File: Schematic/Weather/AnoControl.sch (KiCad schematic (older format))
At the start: 6 parts, among them J10 5_Way_Wire, J11 5_Way_Wire, J12 5_Way_Wire, J13 5_Way_Wire, J8 3_Way_Wire, J9 4_Way_Wire

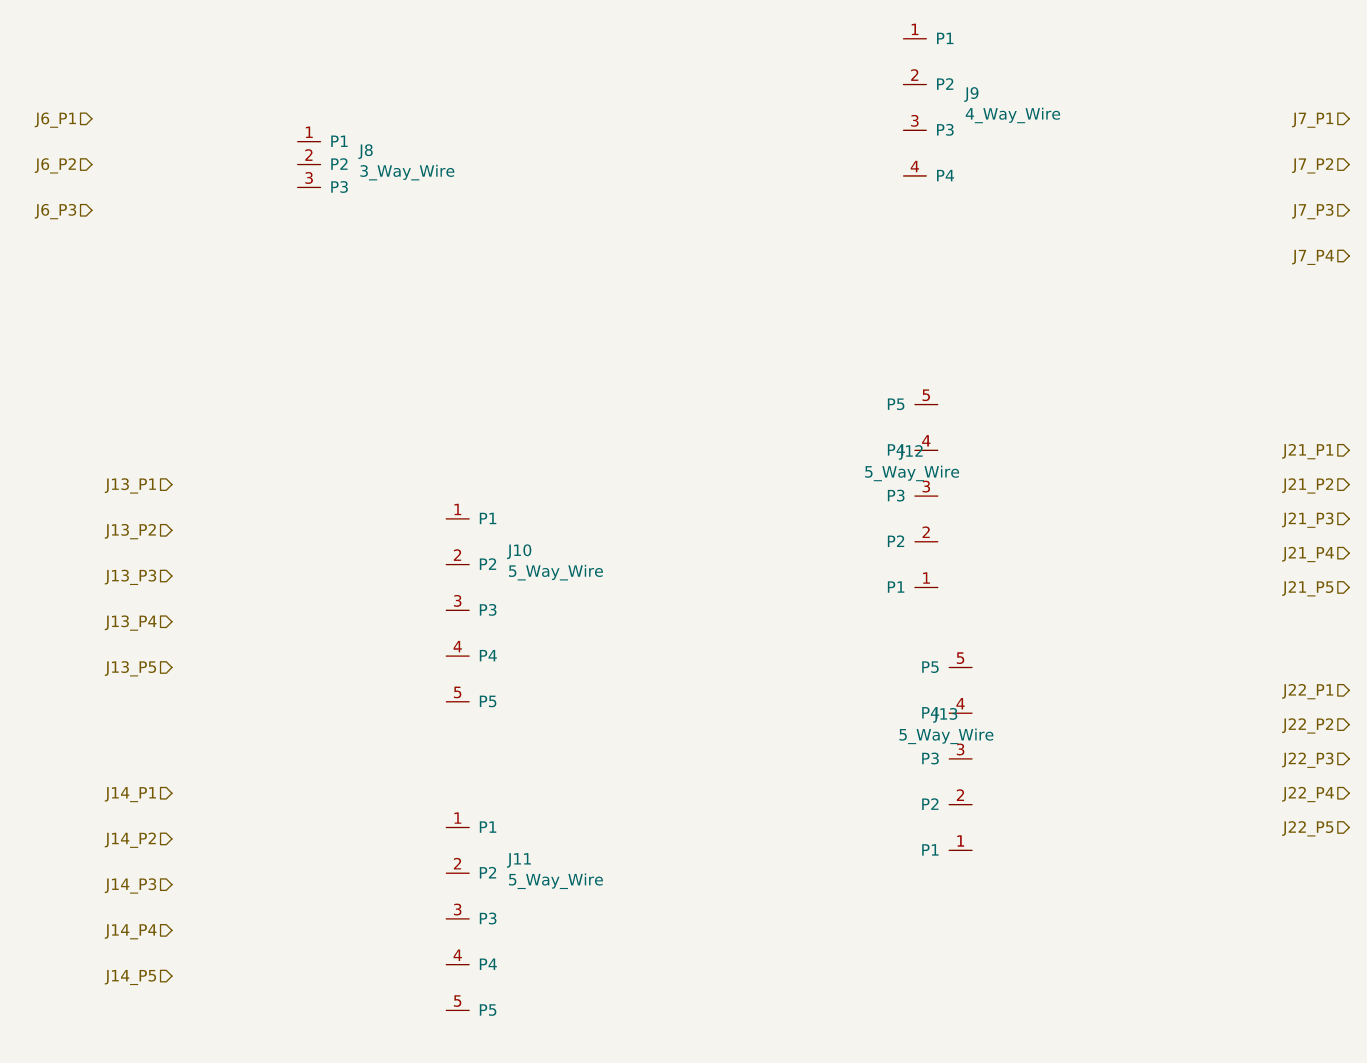
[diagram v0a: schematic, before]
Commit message: Connector changes
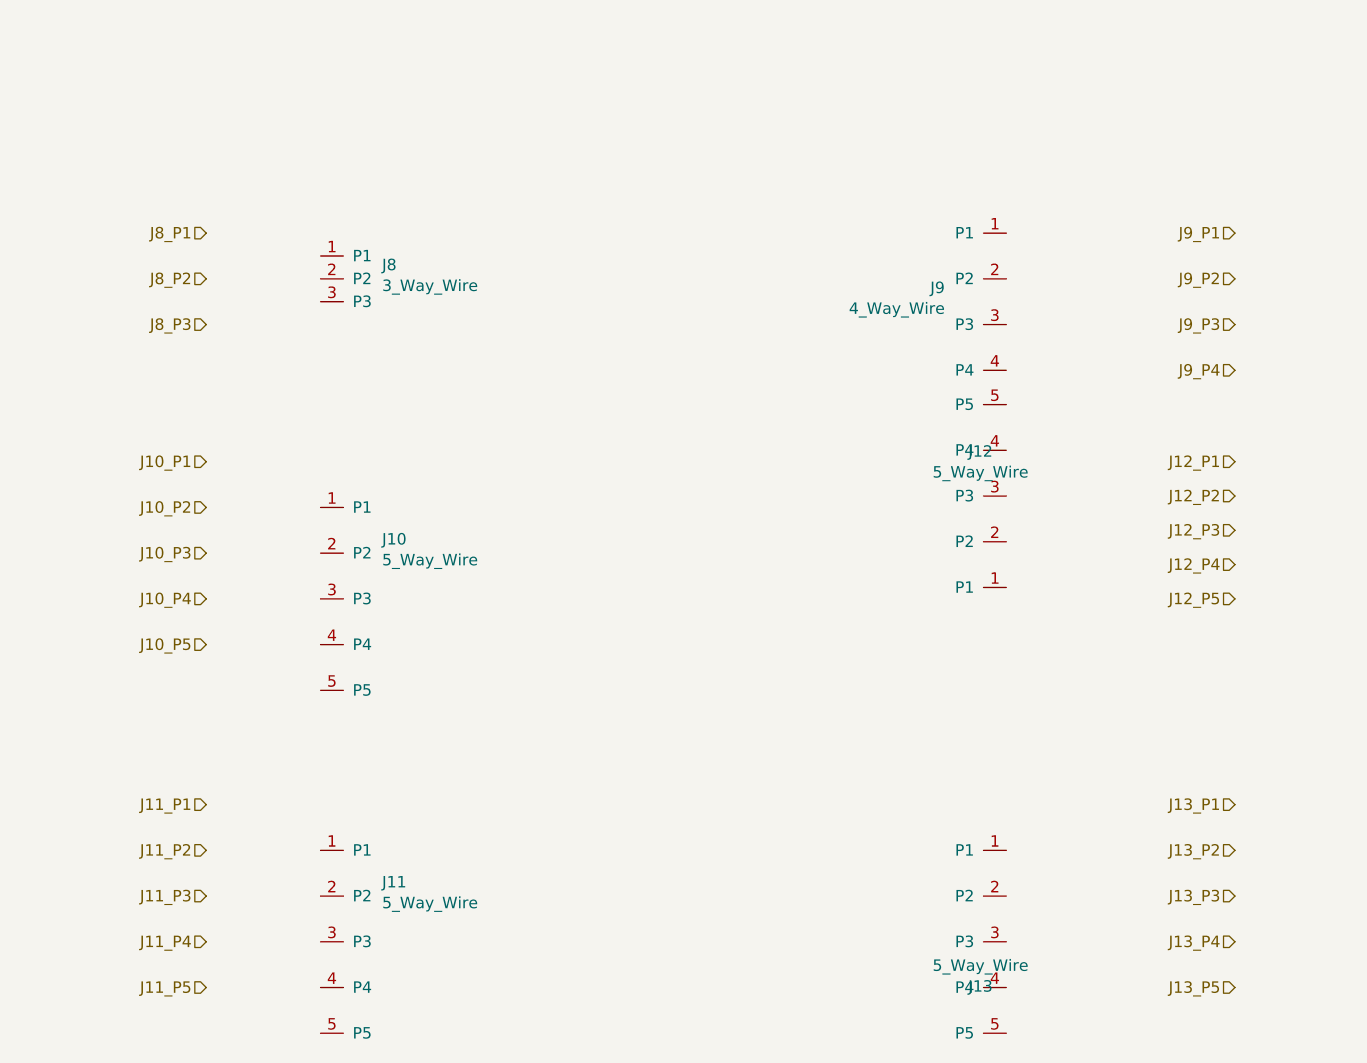
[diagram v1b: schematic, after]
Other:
- moved on the sheet: J10, J11, J12, J13, J8, J9
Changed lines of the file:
@@
 $Descr A4 11693 8268
 encoding utf-8
-Sheet 15 15
+Sheet 13 15
 Title ""
 Date ""
@@
 Comment4 ""
 $EndDescr
-Text HLabel 2500 2000 0    50   Input ~ 0
-J6_P1
-Text HLabel 2500 2200 0    50   Input ~ 0
-J6_P2
-Text HLabel 2500 2400 0    50   Input ~ 0
-J6_P3
-Text HLabel 8000 2000 0    50   Input ~ 0
-J7_P1
-Text HLabel 8000 2200 0    50   Input ~ 0
-J7_P2
-Text HLabel 8000 2400 0    50   Input ~ 0
-J7_P3
-Text HLabel 8000 2600 0    50   Input ~ 0
-J7_P4
-Text HLabel 2850 3600 0    50   Input ~ 0
+Text HLabel 3000 2500 0    50   Input ~ 0
+J8_P1
+Text HLabel 3000 2700 0    50   Input ~ 0
+J8_P2
+Text HLabel 3000 2900 0    50   Input ~ 0
+J8_P3
+Text HLabel 7500 2500 0    50   Input ~ 0
+J9_P1
+Text HLabel 7500 2700 0    50   Input ~ 0
+J9_P2
+Text HLabel 7500 2900 0    50   Input ~ 0
+J9_P3
+Text HLabel 7500 3100 0    50   Input ~ 0
+J9_P4
+Text HLabel 7500 5000 0    50   Input ~ 0
 J13_P1
-Text HLabel 2850 3800 0    50   Input ~ 0
+Text HLabel 7500 5200 0    50   Input ~ 0
 J13_P2
-Text HLabel 2850 4000 0    50   Input ~ 0
+Text HLabel 7500 5400 0    50   Input ~ 0
 J13_P3
-Text HLabel 2850 4200 0    50   Input ~ 0
+Text HLabel 7500 5600 0    50   Input ~ 0
 J13_P4
-Text HLabel 2850 4400 0    50   Input ~ 0
+Text HLabel 7500 5800 0    50   Input ~ 0
 J13_P5
-Text HLabel 2850 4950 0    50   Input ~ 0
-J14_P1
-Text HLabel 2850 5150 0    50   Input ~ 0
-J14_P2
-Text HLabel 2850 5350 0    50   Input ~ 0
-J14_P3
-Text HLabel 2850 5550 0    50   Input ~ 0
-J14_P4
-Text HLabel 2850 5750 0    50   Input ~ 0
-J14_P5
-Text HLabel 8000 3450 0    50   Input ~ 0
-J21_P1
-Text HLabel 8000 3600 0    50   Input ~ 0
-J21_P2
-Text HLabel 8000 3750 0    50   Input ~ 0
-J21_P3
-Text HLabel 8000 3900 0    50   Input ~ 0
-J21_P4
-Text HLabel 8000 4050 0    50   Input ~ 0
-J21_P5
-Text HLabel 8000 4500 0    50   Input ~ 0
-J22_P1
-Text HLabel 8000 4650 0    50   Input ~ 0
-J22_P2
-Text HLabel 8000 4800 0    50   Input ~ 0
-J22_P3
-Text HLabel 8000 4950 0    50   Input ~ 0
-J22_P4
-Text HLabel 8000 5100 0    50   Input ~ 0
-J22_P5
+Text HLabel 3000 5000 0    50   Input ~ 0
+J11_P1
+Text HLabel 3000 5200 0    50   Input ~ 0
+J11_P2
+Text HLabel 3000 5400 0    50   Input ~ 0
+J11_P3
+Text HLabel 3000 5600 0    50   Input ~ 0
+J11_P4
+Text HLabel 3000 5800 0    50   Input ~ 0
+J11_P5
+Text HLabel 7500 3500 0    50   Input ~ 0
+J12_P1
+Text HLabel 7500 3650 0    50   Input ~ 0
+J12_P2
+Text HLabel 7500 3800 0    50   Input ~ 0
+J12_P3
+Text HLabel 7500 3950 0    50   Input ~ 0
+J12_P4
+Text HLabel 7500 4100 0    50   Input ~ 0
+J12_P5
+Text HLabel 3000 3500 0    50   Input ~ 0
+J10_P1
+Text HLabel 3000 3700 0    50   Input ~ 0
+J10_P2
+Text HLabel 3000 3900 0    50   Input ~ 0
+J10_P3
+Text HLabel 3000 4100 0    50   Input ~ 0
+J10_P4
+Text HLabel 3000 4300 0    50   Input ~ 0
+J10_P5
 $Comp
 L MyComponents:4_Way_Wire J9
 U 1 1 5CB50F85
-P 6150 1650
-F 0 "J9" H 6319 1411 50  0000 L CNN
-F 1 "4_Way_Wire" H 6319 1320 50  0000 L CNN
-F 2 "Connector_PinHeader_2.54mm:PinHeader_1x04_P2.54mm_Vertical" H 6050 1700 50  0001 C CNN
-F 3 "" H 6050 1700 50  0001 C CNN
-	1    6150 1650
-	1    0    0    -1
+P 6400 2500
+F 0 "J9" H 6569 2261 50  0000 L CNN
+F 1 "4_Way_Wire" H 6569 2170 50  0000 L CNN
+F 2 "Connector_PinHeader_2.54mm:PinHeader_1x04_P2.54mm_Vertical" H 6300 2550 50  0001 C CNN
+F 3 "" H 6300 2550 50  0001 C CNN
+	1    6400 2500
+	-1   0    0    -1
 $EndComp
 $Comp
 L MyComponents:3_Way_Wire J8
 U 1 1 5CB53FC1
-P 3500 2100
-F 0 "J8" H 3669 2061 50  0000 L CNN
-F 1 "3_Way_Wire" H 3669 1970 50  0000 L CNN
-F 2 "Connector_PinHeader_2.54mm:PinHeader_1x03_P2.54mm_Vertical" H 3500 2100 50  0001 C CNN
-F 3 "" H 3500 2100 50  0001 C CNN
-	1    3500 2100
+P 3600 2600
+F 0 "J8" H 3769 2561 50  0000 L CNN
+F 1 "3_Way_Wire" H 3769 2470 50  0000 L CNN
+F 2 "Connector_PinHeader_2.54mm:PinHeader_1x03_P2.54mm_Vertical" H 3600 2600 50  0001 C CNN
+F 3 "" H 3600 2600 50  0001 C CNN
+	1    3600 2600
 	1    0    0    -1
 $EndComp
@@
 L MyComponents:5_Way_Wire J10
 U 1 1 5CB547B3
-P 4150 3750
-F 0 "J10" H 4319 3611 50  0000 L CNN
-F 1 "5_Way_Wire" H 4319 3520 50  0000 L CNN
-F 2 "Connector_PinHeader_2.54mm:PinHeader_1x05_P2.54mm_Vertical" H 4150 3750 50  0001 C CNN
-F 3 "" H 4150 3750 50  0001 C CNN
-	1    4150 3750
+P 3600 3700
+F 0 "J10" H 3769 3561 50  0000 L CNN
+F 1 "5_Way_Wire" H 3769 3470 50  0000 L CNN
+F 2 "Connector_PinHeader_2.54mm:PinHeader_1x05_P2.54mm_Vertical" H 3600 3700 50  0001 C CNN
+F 3 "" H 3600 3700 50  0001 C CNN
+	1    3600 3700
 	1    0    0    -1
 $EndComp
@@
 L MyComponents:5_Way_Wire J11
 U 1 1 5CB550C8
-P 4150 5100
-F 0 "J11" H 4319 4961 50  0000 L CNN
-F 1 "5_Way_Wire" H 4319 4870 50  0000 L CNN
-F 2 "Connector_PinHeader_2.54mm:PinHeader_1x05_P2.54mm_Vertical" H 4150 5100 50  0001 C CNN
-F 3 "" H 4150 5100 50  0001 C CNN
-	1    4150 5100
+P 3600 5200
+F 0 "J11" H 3769 5061 50  0000 L CNN
+F 1 "5_Way_Wire" H 3769 4970 50  0000 L CNN
+F 2 "Connector_PinHeader_2.54mm:PinHeader_1x05_P2.54mm_Vertical" H 3600 5200 50  0001 C CNN
+F 3 "" H 3600 5200 50  0001 C CNN
+	1    3600 5200
 	1    0    0    -1
 $EndComp
@@
 L MyComponents:5_Way_Wire J12
 U 1 1 5CB55866
-P 6100 4050
-F 0 "J12" H 6113 3455 50  0000 C CNN
-F 1 "5_Way_Wire" H 6113 3546 50  0000 C CNN
-F 2 "Connector_PinHeader_2.54mm:PinHeader_1x05_P2.54mm_Vertical" H 6100 4050 50  0001 C CNN
-F 3 "" H 6100 4050 50  0001 C CNN
-	1    6100 4050
+P 6400 4050
+F 0 "J12" H 6413 3455 50  0000 C CNN
+F 1 "5_Way_Wire" H 6413 3546 50  0000 C CNN
+F 2 "Connector_PinHeader_2.54mm:PinHeader_1x05_P2.54mm_Vertical" H 6400 4050 50  0001 C CNN
+F 3 "" H 6400 4050 50  0001 C CNN
+	1    6400 4050
 	-1   0    0    1
 $EndComp
@@
 L MyComponents:5_Way_Wire J13
 U 1 1 5CB5681F
-P 6250 5200
-F 0 "J13" H 6263 4605 50  0000 C CNN
-F 1 "5_Way_Wire" H 6263 4696 50  0000 C CNN
-F 2 "Connector_PinHeader_2.54mm:PinHeader_1x05_P2.54mm_Vertical" H 6250 5200 50  0001 C CNN
-F 3 "" H 6250 5200 50  0001 C CNN
-	1    6250 5200
-	-1   0    0    1
+P 6400 5200
+F 0 "J13" H 6413 4605 50  0000 C CNN
+F 1 "5_Way_Wire" H 6413 4696 50  0000 C CNN
+F 2 "Connector_PinHeader_2.54mm:PinHeader_1x05_P2.54mm_Vertical" H 6400 5200 50  0001 C CNN
+F 3 "" H 6400 5200 50  0001 C CNN
+	1    6400 5200
+	-1   0    0    -1
 $EndComp
 $EndSCHEMATC

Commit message: config connectors sda scl
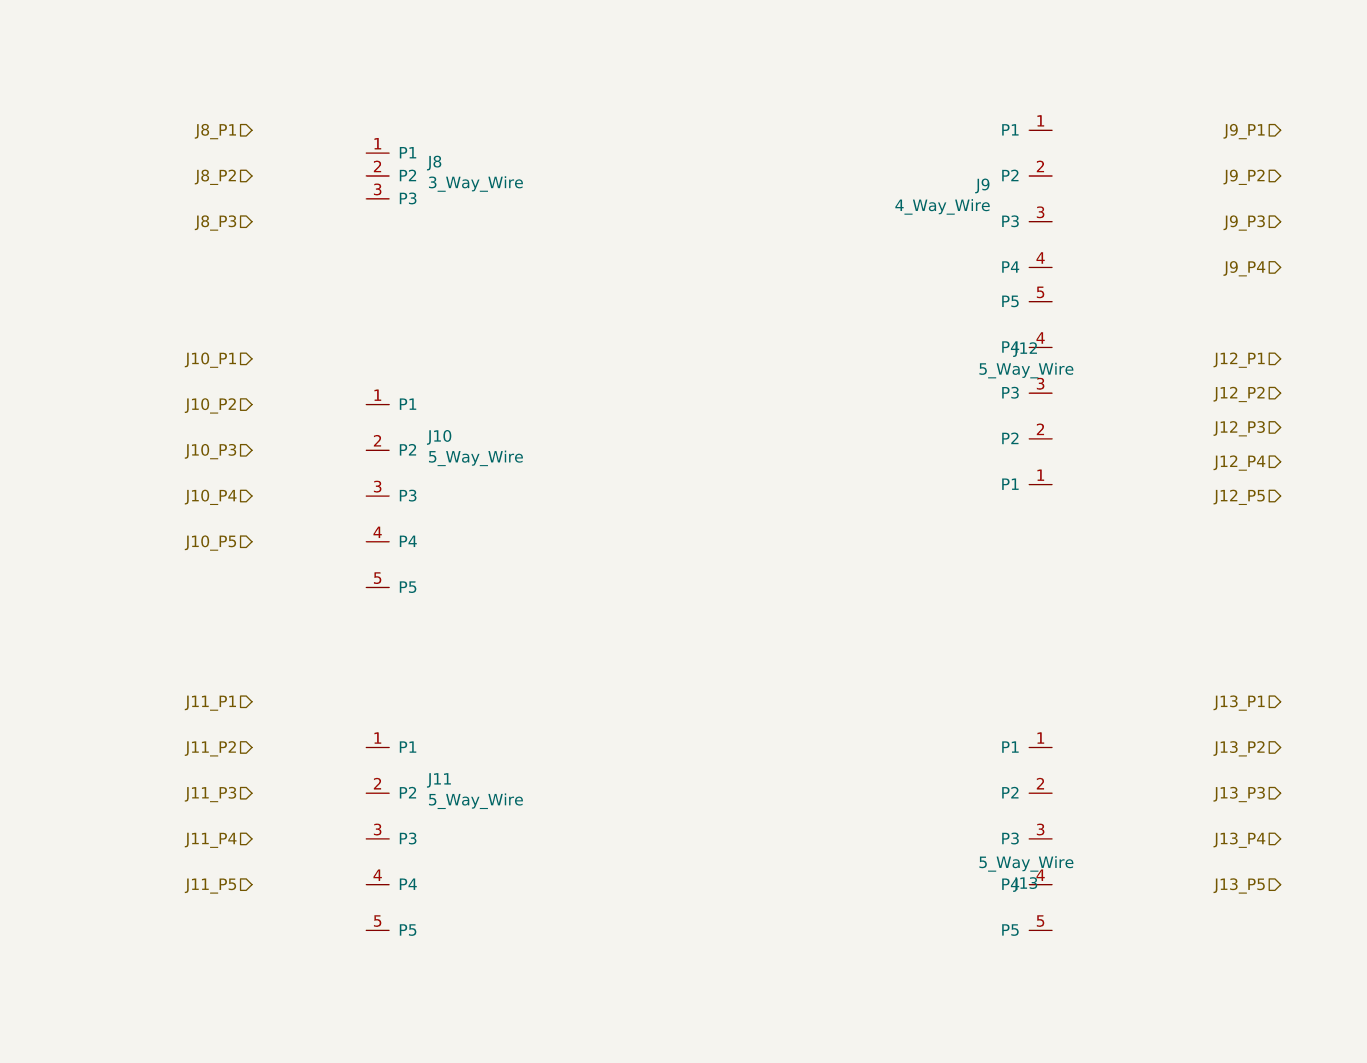
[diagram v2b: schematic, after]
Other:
- moved on the sheet: J10, J11, J12, J13, J8, J9
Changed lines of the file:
@@
 Comment4 ""
 $EndDescr
-Text HLabel 3000 2500 0    50   Input ~ 0
+Text HLabel 3200 2050 0    50   Input ~ 0
 J8_P1
-Text HLabel 3000 2700 0    50   Input ~ 0
+Text HLabel 3200 2250 0    50   Input ~ 0
 J8_P2
-Text HLabel 3000 2900 0    50   Input ~ 0
+Text HLabel 3200 2450 0    50   Input ~ 0
 J8_P3
-Text HLabel 7500 2500 0    50   Input ~ 0
+Text HLabel 7700 2050 0    50   Input ~ 0
 J9_P1
-Text HLabel 7500 2700 0    50   Input ~ 0
+Text HLabel 7700 2250 0    50   Input ~ 0
 J9_P2
-Text HLabel 7500 2900 0    50   Input ~ 0
+Text HLabel 7700 2450 0    50   Input ~ 0
 J9_P3
-Text HLabel 7500 3100 0    50   Input ~ 0
+Text HLabel 7700 2650 0    50   Input ~ 0
 J9_P4
-Text HLabel 7500 5000 0    50   Input ~ 0
+Text HLabel 7700 4550 0    50   Input ~ 0
 J13_P1
-Text HLabel 7500 5200 0    50   Input ~ 0
+Text HLabel 7700 4750 0    50   Input ~ 0
 J13_P2
-Text HLabel 7500 5400 0    50   Input ~ 0
+Text HLabel 7700 4950 0    50   Input ~ 0
 J13_P3
-Text HLabel 7500 5600 0    50   Input ~ 0
+Text HLabel 7700 5150 0    50   Input ~ 0
 J13_P4
-Text HLabel 7500 5800 0    50   Input ~ 0
+Text HLabel 7700 5350 0    50   Input ~ 0
 J13_P5
-Text HLabel 3000 5000 0    50   Input ~ 0
+Text HLabel 3200 4550 0    50   Input ~ 0
 J11_P1
-Text HLabel 3000 5200 0    50   Input ~ 0
+Text HLabel 3200 4750 0    50   Input ~ 0
 J11_P2
-Text HLabel 3000 5400 0    50   Input ~ 0
+Text HLabel 3200 4950 0    50   Input ~ 0
 J11_P3
-Text HLabel 3000 5600 0    50   Input ~ 0
+Text HLabel 3200 5150 0    50   Input ~ 0
 J11_P4
-Text HLabel 3000 5800 0    50   Input ~ 0
+Text HLabel 3200 5350 0    50   Input ~ 0
 J11_P5
-Text HLabel 7500 3500 0    50   Input ~ 0
+Text HLabel 7700 3050 0    50   Input ~ 0
 J12_P1
-Text HLabel 7500 3650 0    50   Input ~ 0
+Text HLabel 7700 3200 0    50   Input ~ 0
 J12_P2
-Text HLabel 7500 3800 0    50   Input ~ 0
+Text HLabel 7700 3350 0    50   Input ~ 0
 J12_P3
-Text HLabel 7500 3950 0    50   Input ~ 0
+Text HLabel 7700 3500 0    50   Input ~ 0
 J12_P4
-Text HLabel 7500 4100 0    50   Input ~ 0
+Text HLabel 7700 3650 0    50   Input ~ 0
 J12_P5
-Text HLabel 3000 3500 0    50   Input ~ 0
+Text HLabel 3200 3050 0    50   Input ~ 0
 J10_P1
-Text HLabel 3000 3700 0    50   Input ~ 0
+Text HLabel 3200 3250 0    50   Input ~ 0
 J10_P2
-Text HLabel 3000 3900 0    50   Input ~ 0
+Text HLabel 3200 3450 0    50   Input ~ 0
 J10_P3
-Text HLabel 3000 4100 0    50   Input ~ 0
+Text HLabel 3200 3650 0    50   Input ~ 0
 J10_P4
-Text HLabel 3000 4300 0    50   Input ~ 0
+Text HLabel 3200 3850 0    50   Input ~ 0
 J10_P5
 $Comp
 L MyComponents:4_Way_Wire J9
 U 1 1 5CB50F85
-P 6400 2500
-F 0 "J9" H 6569 2261 50  0000 L CNN
-F 1 "4_Way_Wire" H 6569 2170 50  0000 L CNN
-F 2 "Connector_PinHeader_2.54mm:PinHeader_1x04_P2.54mm_Vertical" H 6300 2550 50  0001 C CNN
-F 3 "" H 6300 2550 50  0001 C CNN
-	1    6400 2500
+P 6600 2050
+F 0 "J9" H 6769 1811 50  0000 L CNN
+F 1 "4_Way_Wire" H 6769 1720 50  0000 L CNN
+F 2 "Connector_PinHeader_2.54mm:PinHeader_1x04_P2.54mm_Vertical" H 6500 2100 50  0001 C CNN
+F 3 "" H 6500 2100 50  0001 C CNN
+	1    6600 2050
 	-1   0    0    -1
 $EndComp
@@
 L MyComponents:3_Way_Wire J8
 U 1 1 5CB53FC1
-P 3600 2600
-F 0 "J8" H 3769 2561 50  0000 L CNN
-F 1 "3_Way_Wire" H 3769 2470 50  0000 L CNN
-F 2 "Connector_PinHeader_2.54mm:PinHeader_1x03_P2.54mm_Vertical" H 3600 2600 50  0001 C CNN
-F 3 "" H 3600 2600 50  0001 C CNN
-	1    3600 2600
+P 3800 2150
+F 0 "J8" H 3969 2111 50  0000 L CNN
+F 1 "3_Way_Wire" H 3969 2020 50  0000 L CNN
+F 2 "Connector_PinHeader_2.54mm:PinHeader_1x03_P2.54mm_Vertical" H 3800 2150 50  0001 C CNN
+F 3 "" H 3800 2150 50  0001 C CNN
+	1    3800 2150
 	1    0    0    -1
 $EndComp
@@
 L MyComponents:5_Way_Wire J10
 U 1 1 5CB547B3
-P 3600 3700
-F 0 "J10" H 3769 3561 50  0000 L CNN
-F 1 "5_Way_Wire" H 3769 3470 50  0000 L CNN
-F 2 "Connector_PinHeader_2.54mm:PinHeader_1x05_P2.54mm_Vertical" H 3600 3700 50  0001 C CNN
-F 3 "" H 3600 3700 50  0001 C CNN
-	1    3600 3700
+P 3800 3250
+F 0 "J10" H 3969 3111 50  0000 L CNN
+F 1 "5_Way_Wire" H 3969 3020 50  0000 L CNN
+F 2 "Connector_PinHeader_2.54mm:PinHeader_1x05_P2.54mm_Vertical" H 3800 3250 50  0001 C CNN
+F 3 "" H 3800 3250 50  0001 C CNN
+	1    3800 3250
 	1    0    0    -1
 $EndComp
@@
 L MyComponents:5_Way_Wire J11
 U 1 1 5CB550C8
-P 3600 5200
-F 0 "J11" H 3769 5061 50  0000 L CNN
-F 1 "5_Way_Wire" H 3769 4970 50  0000 L CNN
-F 2 "Connector_PinHeader_2.54mm:PinHeader_1x05_P2.54mm_Vertical" H 3600 5200 50  0001 C CNN
-F 3 "" H 3600 5200 50  0001 C CNN
-	1    3600 5200
+P 3800 4750
+F 0 "J11" H 3969 4611 50  0000 L CNN
+F 1 "5_Way_Wire" H 3969 4520 50  0000 L CNN
+F 2 "Connector_PinHeader_2.54mm:PinHeader_1x05_P2.54mm_Vertical" H 3800 4750 50  0001 C CNN
+F 3 "" H 3800 4750 50  0001 C CNN
+	1    3800 4750
 	1    0    0    -1
 $EndComp
@@
 L MyComponents:5_Way_Wire J12
 U 1 1 5CB55866
-P 6400 4050
-F 0 "J12" H 6413 3455 50  0000 C CNN
-F 1 "5_Way_Wire" H 6413 3546 50  0000 C CNN
-F 2 "Connector_PinHeader_2.54mm:PinHeader_1x05_P2.54mm_Vertical" H 6400 4050 50  0001 C CNN
-F 3 "" H 6400 4050 50  0001 C CNN
-	1    6400 4050
+P 6600 3600
+F 0 "J12" H 6613 3005 50  0000 C CNN
+F 1 "5_Way_Wire" H 6613 3096 50  0000 C CNN
+F 2 "Connector_PinHeader_2.54mm:PinHeader_1x05_P2.54mm_Vertical" H 6600 3600 50  0001 C CNN
+F 3 "" H 6600 3600 50  0001 C CNN
+	1    6600 3600
 	-1   0    0    1
 $EndComp
@@
 L MyComponents:5_Way_Wire J13
 U 1 1 5CB5681F
-P 6400 5200
-F 0 "J13" H 6413 4605 50  0000 C CNN
-F 1 "5_Way_Wire" H 6413 4696 50  0000 C CNN
-F 2 "Connector_PinHeader_2.54mm:PinHeader_1x05_P2.54mm_Vertical" H 6400 5200 50  0001 C CNN
-F 3 "" H 6400 5200 50  0001 C CNN
-	1    6400 5200
+P 6600 4750
+F 0 "J13" H 6613 4155 50  0000 C CNN
+F 1 "5_Way_Wire" H 6613 4246 50  0000 C CNN
+F 2 "Connector_PinHeader_2.54mm:PinHeader_1x05_P2.54mm_Vertical" H 6600 4750 50  0001 C CNN
+F 3 "" H 6600 4750 50  0001 C CNN
+	1    6600 4750
 	-1   0    0    -1
 $EndComp
